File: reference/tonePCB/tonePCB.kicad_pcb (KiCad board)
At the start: 2 copper layers, 40.6 x 66 mm, 15 parts, among them J1 to_ftdi, U1 ATMEGA328P-PU

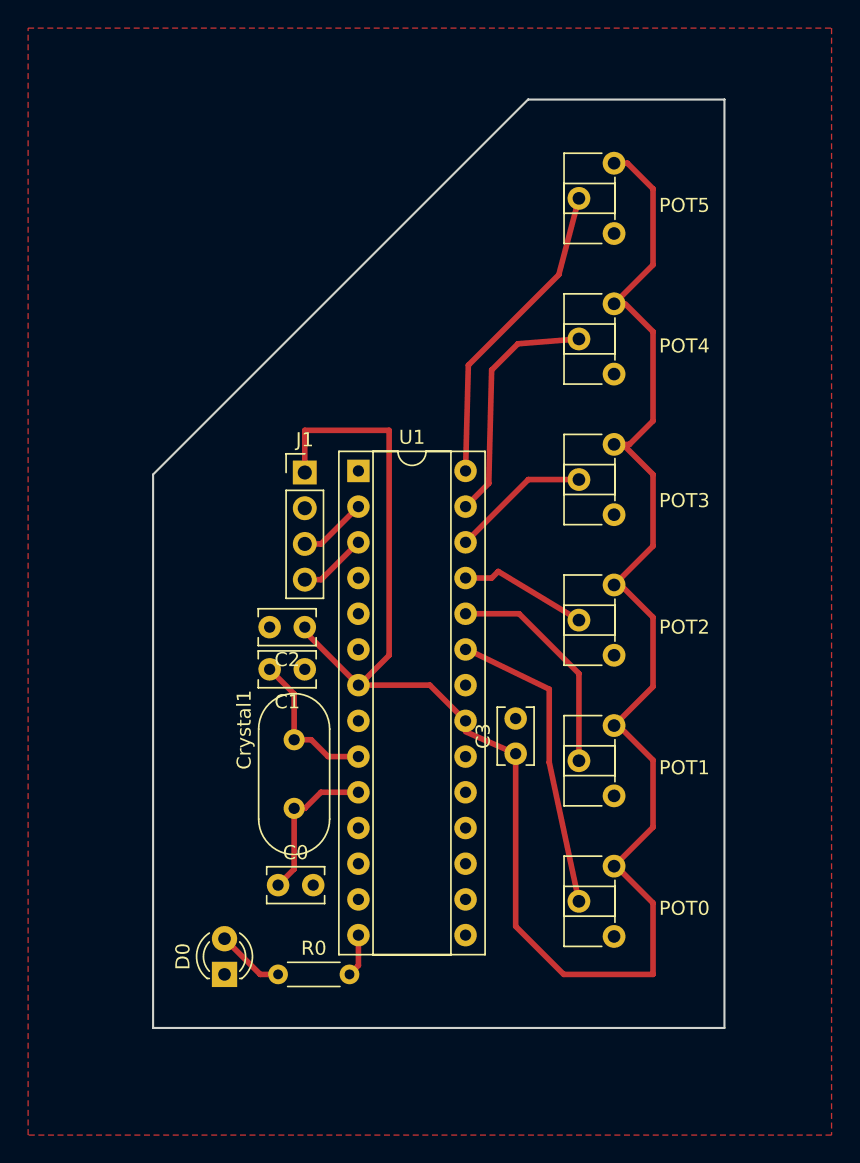
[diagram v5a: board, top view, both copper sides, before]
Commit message: Reshaping the board to a rectangle
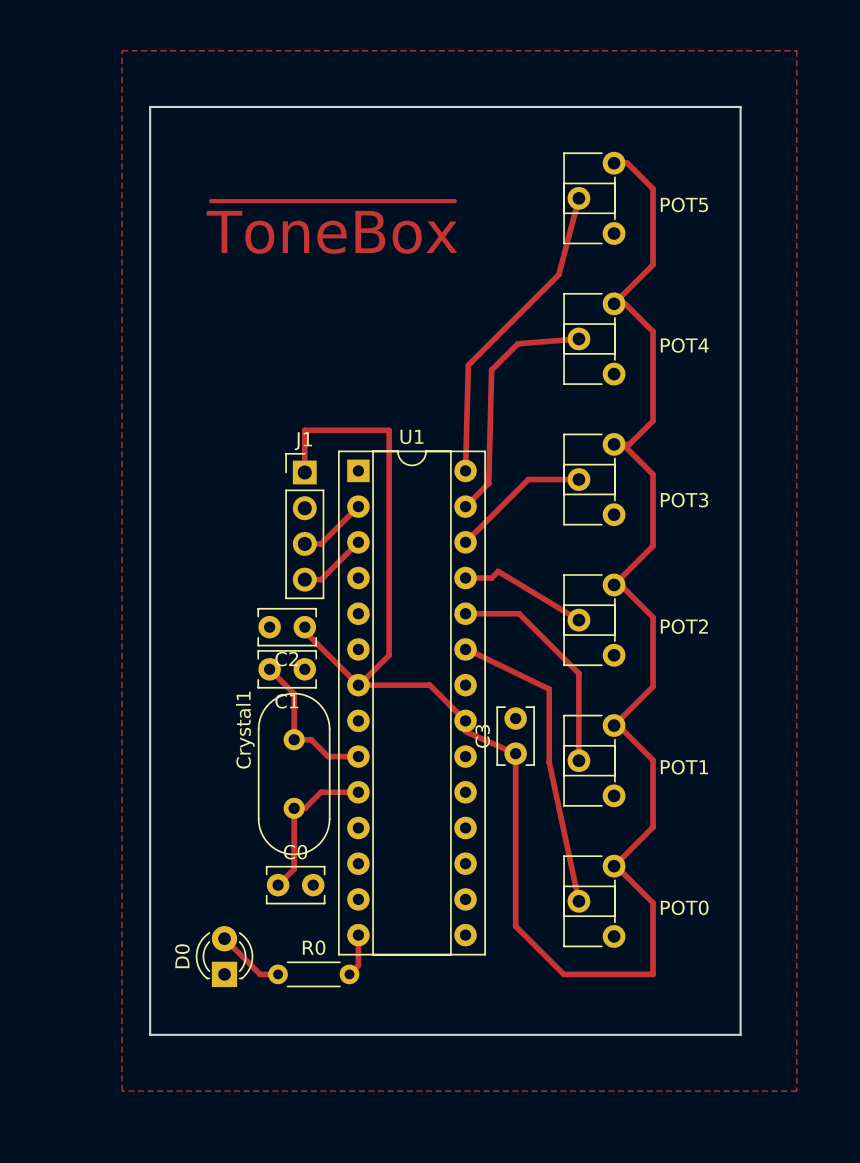
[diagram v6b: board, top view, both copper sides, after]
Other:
- board size 40.6 x 66 mm -> 42 x 66 mm
- board text added: "~ToneBox~"
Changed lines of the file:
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@@
     (visible_elements FFFFFF7F)
     (pcbplotparams
-      (layerselection 0x00000_80000001)
+      (layerselection 0x01000_00000001)
       (usegerberextensions false)
       (excludeedgelayer true)
@@
     )
   )
-  (gr_line (start 156.21 104.14) (end 156.21 143.51) (angle 90) (layer Edge.Cuts) (width 0.15))
-  (gr_line (start 182.88 77.47) (end 156.21 104.14) (angle 90) (layer Edge.Cuts) (width 0.15))
-  (gr_line (start 196.85 77.47) (end 182.88 77.47) (angle 90) (layer Edge.Cuts) (width 0.15))
-  (gr_line (start 196.85 143.51) (end 196.85 77.47) (angle 90) (layer Edge.Cuts) (width 0.15))
-  (gr_line (start 156.21 143.51) (end 196.85 143.51) (angle 90) (layer Edge.Cuts) (width 0.15))
+  (gr_text ~ToneBox~ (at 169 87) (layer F.Cu)
+    (effects (font (size 3 3) (thickness 0.3)))
+  )
+  (gr_line (start 198 144) (end 198 78) (angle 90) (layer Edge.Cuts) (width 0.15))
+  (gr_line (start 156 144) (end 198 144) (angle 90) (layer Edge.Cuts) (width 0.15))
+  (gr_line (start 156 78) (end 156 144) (angle 90) (layer Edge.Cuts) (width 0.15))
+  (gr_line (start 198 78) (end 156 78) (angle 90) (layer Edge.Cuts) (width 0.15))
   (segment (start 166.243 127.889) (end 166.243 132.207) (width 0.4) (layer F.Cu) (net 1))
   (segment (start 166.243 132.207) (end 165.1 133.35) (width 0.4) (layer F.Cu) (net 1))
@@
     (polygon
       (pts
-        (xy 204.47 151.13) (xy 147.32 151.13) (xy 147.32 72.39) (xy 204.47 72.39)
+        (xy 202 148) (xy 154 148) (xy 154 74) (xy 202 74)
       )
     )

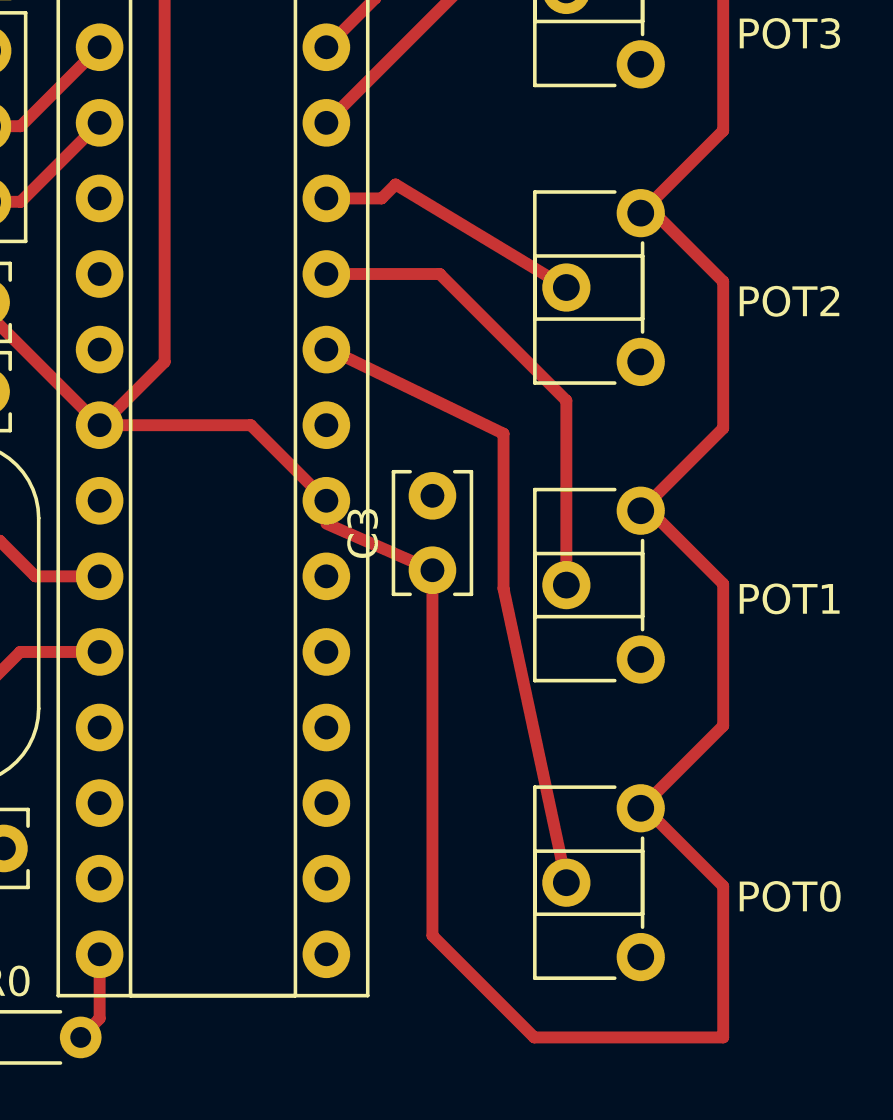
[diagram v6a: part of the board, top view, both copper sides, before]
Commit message: Widening the clearance between the tracks and the ground pour
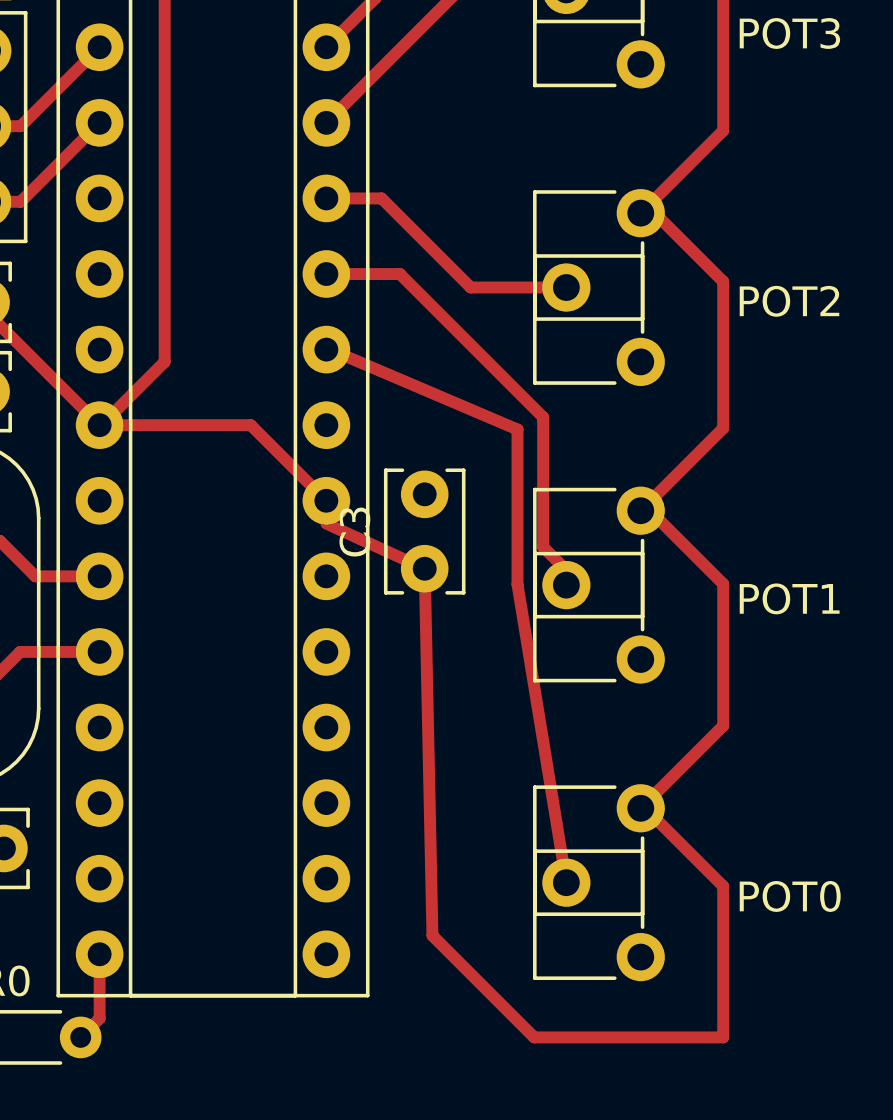
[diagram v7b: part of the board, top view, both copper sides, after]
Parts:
- moved C3 0.26 mm to (181.7, 124.0)
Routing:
- net Net-(POT1-Pad2): track 16.0 -> 15.2 mm
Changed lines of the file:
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@@
     (links 37)
     (no_connects 0)
-    (area 154.94 74.93 198.120001 144.780001)
+    (area 154 74 202.000001 148.000001)
     (thickness 1.6)
     (drawings 5)
-    (tracks 89)
+    (tracks 92)
     (zones 0)
     (modules 15)
@@
     (user_trace_width 0.4)
     (trace_clearance 0.2)
-    (zone_clearance 0.508)
+    (zone_clearance 0.75)
     (zone_45_only no)
     (trace_min 0.2)
@@
   )
   (module Capacitors_THT:C_Rect_L4.0mm_W2.5mm_P2.50mm (layer F.Cu)
-    (at 182 124 90)
+    (at 181.74 123.95 90)
     (descr "C, Rect series, Radial, pin pitch=2.50mm, , length*width=4*2.5mm^2, Capacitor")
     (tags "C Rect series Radial pin pitch 2.50mm  length 4mm width 2.5mm Capacitor")
@@
   (segment (start 167.459 123.009) (end 168.656 124.206) (width 0.4) (layer F.Cu) (net 3))
   (segment (start 168.656 124.206) (end 170.815 124.206) (width 0.4) (layer F.Cu) (net 3))
-  (segment (start 182 136.28) (end 182 124) (width 0.4) (layer F.Cu) (net 4))
+  (segment (start 182 136.28) (end 181.74 123.95) (width 0.4) (layer F.Cu) (net 4) (status 20))
   (segment (start 189.15 132) (end 191.77 134.62) (width 0.4) (layer F.Cu) (net 4))
   (segment (start 191.77 134.62) (end 191.77 139.7) (width 0.4) (layer F.Cu) (net 4))
@@
   (segment (start 170.874 119.126) (end 170.815 119.126) (width 0.25) (layer F.Cu) (net 4))
   (segment (start 178.435 121.666) (end 178.435 122.435) (width 0.25) (layer F.Cu) (net 4))
-  (segment (start 178.435 122.435) (end 182 124) (width 0.4) (layer F.Cu) (net 4) (status 20))
+  (segment (start 178.435 122.435) (end 181.74 123.95) (width 0.4) (layer F.Cu) (net 4) (status 20))
   (segment (start 167 115) (end 167 115.311) (width 0.25) (layer F.Cu) (net 4))
   (segment (start 167 115.311) (end 170.815 119.126) (width 0.4) (layer F.Cu) (net 4))
@@
   (segment (start 189 92) (end 189 92.047) (width 0.25) (layer F.Cu) (net 4) (status 30))
   (segment (start 189 82) (end 189 82.047) (width 0.25) (layer F.Cu) (net 4) (status 30))
-  (segment (start 178.562 116.586) (end 184.388 119.412) (width 0.4) (layer F.Cu) (net 5))
+  (segment (start 178.562 116.586) (end 184.858 119.272) (width 0.4) (layer F.Cu) (net 5))
   (segment (start 178.435 116.586) (end 178.562 116.586) (width 0.25) (layer F.Cu) (net 5))
-  (segment (start 184.388 124.619) (end 186.5 134.5) (width 0.4) (layer F.Cu) (net 5) (status 20))
-  (segment (start 184.388 119.412) (end 184.388 124.619) (width 0.4) (layer F.Cu) (net 5))
-  (segment (start 186.5 124.5) (end 186.5 118.3) (width 0.4) (layer F.Cu) (net 6))
-  (segment (start 182.246 114.046) (end 178.435 114.046) (width 0.4) (layer F.Cu) (net 6))
-  (segment (start 186.5 118.3) (end 182.246 114.046) (width 0.4) (layer F.Cu) (net 6))
-  (segment (start 186.5 114.5) (end 180.761 111.038) (width 0.4) (layer F.Cu) (net 7) (status 10))
-  (segment (start 180.761 111.038) (end 180.293 111.506) (width 0.4) (layer F.Cu) (net 7))
+  (segment (start 184.858 124.479) (end 186.5 134.5) (width 0.4) (layer F.Cu) (net 5) (status 20))
+  (segment (start 184.858 119.272) (end 184.858 124.479) (width 0.4) (layer F.Cu) (net 5))
+  (segment (start 185.72 118.94) (end 185.72 118.86) (width 0.4) (layer F.Cu) (net 6))
+  (segment (start 185.72 123.22) (end 185.72 118.94) (width 0.4) (layer F.Cu) (net 6))
+  (segment (start 186.5 124) (end 185.72 123.22) (width 0.4) (layer F.Cu) (net 6))
+  (segment (start 180.906 114.046) (end 178.435 114.046) (width 0.4) (layer F.Cu) (net 6))
+  (segment (start 185.72 118.86) (end 180.906 114.046) (width 0.4) (layer F.Cu) (net 6))
+  (segment (start 186.5 124.5) (end 186.5 124) (width 0.4) (layer F.Cu) (net 6))
+  (segment (start 186.5 114.5) (end 183.287 114.5) (width 0.4) (layer F.Cu) (net 7))
   (segment (start 180.293 111.506) (end 178.435 111.506) (width 0.4) (layer F.Cu) (net 7))
+  (segment (start 183.287 114.5) (end 180.293 111.506) (width 0.4) (layer F.Cu) (net 7))
   (segment (start 186.5 104.5) (end 182.901 104.5) (width 0.4) (layer F.Cu) (net 8))
   (segment (start 182.901 104.5) (end 178.435 108.966) (width 0.4) (layer F.Cu) (net 8))
@@
   (segment (start 170.815 139.065) (end 170.18 139.7) (width 0.4) (layer F.Cu) (net 27))
   (zone (net 2) (net_name Earth) (layer F.Cu) (hatch edge 0.508)
-    (connect_pads (clearance 0.508))
+    (connect_pads (clearance 0.75))
     (min_thickness 0.254)
     (fill yes (arc_segments 16) (thermal_gap 0.508) (thermal_bridge_width 0.508))
